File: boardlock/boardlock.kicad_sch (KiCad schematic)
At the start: 48 parts, among them U1 ESP32-S3-WROOM-1

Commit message: footprints finished for now
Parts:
- removed U1: ESP32-S3-WROOM-1, PCM_Espressif:ESP32-S3-WROOM-1, symbol PCM_Espressif:ESP32-S3-WROOM-1
- added U10: ESP32-S3-WROOM-1, espressif-kicad:ESP32-S3-WROOM-1, symbol Espressif:ESP32-S3-WROOM-1
- H1, H2, H3, H4: footprint (none) -> MountingHole:MountingHole_2.2mm_M2
- TP10, TP11, TP12, TP13, TP14, TP15, TP16, TP17, TP18, TP19, TP20, TP22, TP23, TP24, TP25, TP26, TP27, TP28, TP29, TP31, TP32, TP35, TP36, TP37, TP38, TP39, TP4, TP41, TP42, TP7, TP8, TP9: footprint (none) -> TestPoint:TestPoint_Pad_D1.0mm
- TP30, TP33, TP34, TP5: footprint TestPoint:TestPoint_Plated_Hole_D3.0mm -> TestPoint:TestPoint_Pad_D1.0mm
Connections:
- net +3V3: now also U10.2 (3V3)
- net GND: now also U10.1 (GND), U10.40 (GND), U10.41 (GND)
- net M_AUDIO_SD_MODE: now also U10.9 (GPIO16/U0CTS/ADC2_CH5/XTAL_32K_N)
- net M_BOOST_EN: now also U10.24 (GPIO47/SPICLK_P/SUBSPICLK_P_DIFF)
- net M_BOOT: now also U10.27 (GPIO0/BOOT)
- net M_BUTTON_EXT1: now also U10.39 (GPIO1/TOUCH1/ADC1_CH0)
- net M_BUTTON_EXT2: now also U10.38 (GPIO2/TOUCH2/ADC1_CH1)
- net M_BUTTON_INT: now also U10.31 (GPIO38/FSPIWP/SUBSPIWP)
- net M_BUZZER: now also U10.25 (GPIO48/SPICLK_N/SUBSPICLK_N_DIFF)
- net M_FUEL_GPOUT: now also U10.8 (GPIO15/U0RTS/ADC2_CH4/XTAL_32K_P)
- net M_GPS_EXTINT: now also U10.23 (GPIO21)
- net M_GPS_POWER: now also U10.22 (GPIO14/TOUCH14/ADC2_CH3/FSPIWP/FSPIDQS/SUBSPIWP)
- net M_HEARTBEAT: now also U10.30 (SPIDQS/GPIO37/FSPIQ/SUBSPIQ)
- net M_I2C_SCL: now also U10.17 (GPIO9/TOUCH9/ADC1_CH8/FSPIHD/SUBSPIHD)
- net M_I2C_SDA: now also U10.12 (GPIO8/TOUCH8/ADC1_CH7/SUBSPICS1)
- net M_I2S_BCLK: now also U10.6 (GPIO6/TOUCH6/ADC1_CH5)
- net M_I2S_Data_Out: now also U10.5 (GPIO5/TOUCH5/ADC1_CH4)
- net M_I2S_LRC: now also U10.7 (GPIO7/TOUCH7/ADC1_CH6)
- net M_IMU_INT2: now also U10.28 (SPIIO6/GPIO35/FSPID/SUBSPID)
- net M_IMU_POWER: now also U10.4 (GPIO4/TOUCH4/ADC1_CH3)
- net M_RGB_B: now also U10.35 (MTMS/GPIO42)
- net M_RGB_G: now also U10.34 (MTDI/GPIO41/CLK_OUT1)
- net M_RGB_R: now also U10.33 (MTDO/GPIO40/CLK_OUT2)
- net M_RST_N: now also U10.3 (EN)
- net M_SPI_CLK: now also U10.20 (GPIO12/TOUCH12/ADC2_CH1/FSPICLK/FSPIIO6/SUBSPICLK)
- net M_SPI_CS: now also U10.18 (GPIO10/TOUCH10/ADC1_CH9/FSPICS0/FSPIIO4/SUBSPICS0)
- net M_SPI_MISO: now also U10.21 (GPIO13/TOUCH13/ADC2_CH2/FSPIQ/FSPIIO7/SUBSPIQ)
- net M_SPI_MOSI: now also U10.19 (GPIO11/TOUCH11/ADC2_CH0/FSPID/FSPIIO5/SUBSPID)
- net M_UART_RX: now also U10.11 (GPIO18/U1RXD/ADC2_CH7/CLK_OUT3)
- net M_UART_TX: now also U10.10 (GPIO17/U1TXD/ADC2_CH6)
- net M_USB_D+: now also U10.14 (GPIO20/U1CTS/ADC2_CH9/CLK_OUT1/USB_D+)
- net M_USB_D-: now also U10.13 (GPIO19/U1RTS/ADC2_CH8/CLK_OUT2/USB_D-)
- net at TP31.1: now also U10.37 (U0TXD/GPIO43/CLK_OUT1)
- net at TP33.1: now also U10.16 (GPIO46)
- net at TP34.1: now also U10.15 (GPIO3/TOUCH3/ADC1_CH2)
- net at TP30.1: now also U10.26 (GPIO45)
- net at TP6.1: now also U10.29 (SPIIO7/GPIO36/FSPICLK/SUBSPICLK)
- net at TP5.1: now also U10.32 (MTCK/GPIO39/CLK_OUT3/SUBSPICS1)
- net at TP32.1: now also U10.36 (U0RXD/GPIO44/CLK_OUT2)

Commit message: Nick PCB edits
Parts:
- added R? (x2): 0, Resistor_SMD:R_0805_2012Metric_Pad1.20x1.40mm_HandSolder, symbol Device:R_US
- added TP40, TP43: TestPoint, TestPoint:TestPoint_Pad_D1.0mm, symbol Connector:TestPoint
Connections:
- net M_BATT_CHARGE_N_CHG: now also R?.2, TP40.1
- net M_BATT_CHARGE_N_PGOOD: now also R?.2, TP43.1
- net at TP33.1, U10.16 (GPIO46): now also R?.1
- net at TP30.1, U10.26 (GPIO45): now also R?.1
- no-connect marks 2 -> 0
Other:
- moved on the sheet: TP30, TP33
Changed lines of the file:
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@@
   (junction (at 213.36 95.25) (diameter 0) (color 0 0 0 0)
   )
+  (junction (at 208.28 137.16) (diameter 0) (color 0 0 0 0)
+  )
   (junction (at 213.36 106.68) (diameter 0) (color 0 0 0 0)
   )
@@
   (junction (at 124.46 45.72) (diameter 0) (color 0 0 0 0)
   )
+  (junction (at 208.28 134.62) (diameter 0) (color 0 0 0 0)
+  )
+  (junction (at 219.71 134.62) (diameter 0) (color 0 0 0 0)
+  )
   (junction (at 113.03 45.72) (diameter 0) (color 0 0 0 0)
   )
-  (no_connect (at 43.18 34.29))
-  (no_connect (at 40.64 31.75))
+  (junction (at 219.71 137.16) (diameter 0) (color 0 0 0 0)
+  )
   (wire (pts (xy 80.01 142.24) (xy 88.9 142.24))
     (stroke (width 0) (type default))
   )
+  (wire (pts (xy 219.71 134.62) (xy 218.44 134.62))
+    (stroke (width 0) (type default))
+  )
   (wire (pts (xy 180.34 71.12) (xy 182.88 71.12))
     (stroke (width 0) (type default))
   )
+  (wire (pts (xy 220.98 134.62) (xy 219.71 134.62))
+    (stroke (width 0) (type default))
+  )
   (wire (pts (xy 180.34 114.3) (xy 189.23 114.3))
     (stroke (width 0) (type default))
@@
     (stroke (width 0) (type default))
   )
+  (wire (pts (xy 208.28 134.62) (xy 210.82 134.62))
+    (stroke (width 0) (type default))
+  )
   (wire (pts (xy 113.03 45.72) (xy 113.03 48.26))
     (stroke (width 0) (type default))
   )
+  (wire (pts (xy 220.98 137.16) (xy 219.71 137.16))
+    (stroke (width 0) (type default))
+  )
   (wire (pts (xy 180.34 104.14) (xy 189.23 104.14))
     (stroke (width 0) (type default))
@@
     (stroke (width 0) (type default))
   )
+  (wire (pts (xy 219.71 137.16) (xy 219.71 138.43))
+    (stroke (width 0) (type default))
+  )
   (wire (pts (xy 36.83 78.74) (xy 35.56 78.74))
     (stroke (width 0) (type default))
@@
     (stroke (width 0) (type default))
   )
+  (wire (pts (xy 219.71 137.16) (xy 218.44 137.16))
+    (stroke (width 0) (type default))
+  )
+  (wire (pts (xy 208.28 134.62) (xy 208.28 133.35))
+    (stroke (width 0) (type default))
+  )
   (wire (pts (xy 180.34 109.22) (xy 223.52 109.22))
     (stroke (width 0) (type default))
   )
-  (wire (pts (xy 180.34 137.16) (xy 189.23 137.16))
+  (wire (pts (xy 180.34 137.16) (xy 208.28 137.16))
     (stroke (width 0) (type default))
   )
@@
     (stroke (width 0) (type default))
   )
+  (wire (pts (xy 208.28 137.16) (xy 210.82 137.16))
+    (stroke (width 0) (type default))
+  )
   (wire (pts (xy 180.34 142.24) (xy 189.23 142.24))
     (stroke (width 0) (type default))
@@
     (stroke (width 0) (type default))
   )
+  (wire (pts (xy 219.71 134.62) (xy 219.71 133.35))
+    (stroke (width 0) (type default))
+  )
   (wire (pts (xy 252.73 127) (xy 254 127))
     (stroke (width 0) (type default))
@@
     (stroke (width 0) (type default))
   )
-  (wire (pts (xy 180.34 134.62) (xy 189.23 134.62))
+  (wire (pts (xy 180.34 134.62) (xy 208.28 134.62))
+    (stroke (width 0) (type default))
+  )
+  (wire (pts (xy 208.28 137.16) (xy 208.28 138.43))
     (stroke (width 0) (type default))
   )
@@
     )
   )
-  (global_label "M_BATT_CHARGE_N_CHG" (shape input) (at 13.97 31.75 0) (fields_autoplaced)
-    (effects (font (size 1.27 1.27)) (justify left))
-    (property "Intersheetrefs" "${INTERSHEET_REFS}" (at 39.1499 31.75 0)
+  (global_label "M_BATT_CHARGE_N_CHG" (shape input) (at 220.98 134.62 0) (fields_autoplaced)
+    (effects (font (size 1.27 1.27)) (justify left))
+    (property "Intersheetrefs" "${INTERSHEET_REFS}" (at 246.1599 134.62 0)
       (effects (font (size 1.27 1.27)) (justify left) hide)
     )
@@
     )
   )
-  (global_label "M_BATT_CHARGE_N_PGOOD" (shape input) (at 13.97 34.29 0) (fields_autoplaced)
-    (effects (font (size 1.27 1.27)) (justify left))
-    (property "Intersheetrefs" "${INTERSHEET_REFS}" (at 41.7504 34.29 0)
+  (global_label "M_BATT_CHARGE_N_PGOOD" (shape input) (at 220.98 137.16 0) (fields_autoplaced)
+    (effects (font (size 1.27 1.27)) (justify left))
+    (property "Intersheetrefs" "${INTERSHEET_REFS}" (at 248.7604 137.16 0)
       (effects (font (size 1.27 1.27)) (justify left) hide)
     )
@@
     )
   )
-  (symbol (lib_id "Connector:TestPoint") (at 189.23 137.16 270) (unit 1)
-    (in_bom yes) (on_board yes) (dnp no)
-    (property "Reference" "TP33" (at 196.85 137.16 90)
-      (effects (font (size 1.27 1.27)))
-    )
-    (property "Value" "TestPoint" (at 204.47 137.16 90)
-      (effects (font (size 1.27 1.27)))
-    )
-    (property "Footprint" "TestPoint:TestPoint_Pad_D1.0mm" (at 189.23 142.24 0)
-      (effects (font (size 1.27 1.27)) hide)
-    )
-    (property "Datasheet" "~" (at 189.23 142.24 0)
+  (symbol (lib_id "Connector:TestPoint") (at 208.28 138.43 180) (unit 1)
+    (in_bom yes) (on_board yes) (dnp no)
+    (property "Reference" "TP33" (at 208.28 146.05 90)
+      (effects (font (size 1.27 1.27)))
+    )
+    (property "Value" "TestPoint" (at 208.28 153.67 90)
+      (effects (font (size 1.27 1.27)) hide)
+    )
+    (property "Footprint" "TestPoint:TestPoint_Pad_D1.0mm" (at 203.2 138.43 0)
+      (effects (font (size 1.27 1.27)) hide)
+    )
+    (property "Datasheet" "~" (at 203.2 138.43 0)
       (effects (font (size 1.27 1.27)) hide)
     )
@@
     )
   )
+  (symbol (lib_id "Connector:TestPoint") (at 219.71 138.43 180) (unit 1)
+    (in_bom yes) (on_board yes) (dnp no)
+    (property "Reference" "TP43" (at 219.71 146.05 90)
+      (effects (font (size 1.27 1.27)))
+    )
+    (property "Value" "TestPoint" (at 219.71 153.67 90)
+      (effects (font (size 1.27 1.27)) hide)
+    )
+    (property "Footprint" "TestPoint:TestPoint_Pad_D1.0mm" (at 214.63 138.43 0)
+      (effects (font (size 1.27 1.27)) hide)
+    )
+    (property "Datasheet" "~" (at 214.63 138.43 0)
+      (effects (font (size 1.27 1.27)) hide)
+    )
+    (pin "1")
+    (instances
+      (project "boardlock"
+        (path "/e1fc29ce-837e-4062-84d8-c7e423f9eab9"
+          (reference "TP43") (unit 1)
+        )
+      )
+    )
+  )
   (symbol (lib_id "Connector:TestPoint") (at 254 91.44 270) (unit 1)
     (in_bom yes) (on_board yes) (dnp no)
@@
     )
   )
-  (symbol (lib_id "Connector:TestPoint") (at 189.23 134.62 270) (unit 1)
-    (in_bom yes) (on_board yes) (dnp no)
-    (property "Reference" "TP30" (at 196.85 134.62 90)
-      (effects (font (size 1.27 1.27)))
-    )
-    (property "Value" "TestPoint" (at 204.47 134.62 90)
-      (effects (font (size 1.27 1.27)))
-    )
-    (property "Footprint" "TestPoint:TestPoint_Pad_D1.0mm" (at 189.23 139.7 0)
-      (effects (font (size 1.27 1.27)) hide)
-    )
-    (property "Datasheet" "~" (at 189.23 139.7 0)
+  (symbol (lib_id "Connector:TestPoint") (at 208.28 133.35 0) (unit 1)
+    (in_bom yes) (on_board yes) (dnp no)
+    (property "Reference" "TP30" (at 208.28 125.73 90)
+      (effects (font (size 1.27 1.27)))
+    )
+    (property "Value" "TestPoint" (at 208.28 118.11 90)
+      (effects (font (size 1.27 1.27)) hide)
+    )
+    (property "Footprint" "TestPoint:TestPoint_Pad_D1.0mm" (at 213.36 133.35 0)
+      (effects (font (size 1.27 1.27)) hide)
+    )
+    (property "Datasheet" "~" (at 213.36 133.35 0)
       (effects (font (size 1.27 1.27)) hide)
     )
@@
         (path "/e1fc29ce-837e-4062-84d8-c7e423f9eab9"
           (reference "H1") (unit 1)
+        )
+      )
+    )
+  )
+  (symbol (lib_id "Device:R_US") (at 214.63 137.16 90) (unit 1)
+    (in_bom yes) (on_board yes) (dnp no)
+    (property "Reference" "R?" (at 213.36 139.7 90)
+      (effects (font (size 1.27 1.27)))
+    )
+    (property "Value" "0" (at 217.17 139.7 90)
+      (effects (font (size 1.27 1.27)))
+    )
+    (property "Footprint" "Resistor_SMD:R_0805_2012Metric_Pad1.20x1.40mm_HandSolder" (at 214.884 136.144 90)
+      (effects (font (size 1.27 1.27)) hide)
+    )
+    (property "Datasheet" "~" (at 214.63 137.16 0)
+      (effects (font (size 1.27 1.27)) hide)
+    )
+    (pin "1")
+    (pin "2")
+    (instances
+      (project "boardlock"
+        (path "/e1fc29ce-837e-4062-84d8-c7e423f9eab9/a05f4dcd-7a18-4529-a05e-43353e81fbf8"
+          (reference "R?") (unit 1)
+        )
+        (path "/e1fc29ce-837e-4062-84d8-c7e423f9eab9"
+          (reference "R27") (unit 1)
+        )
+      )
+    )
+  )
+  (symbol (lib_id "Connector:TestPoint") (at 219.71 133.35 0) (unit 1)
+    (in_bom yes) (on_board yes) (dnp no)
+    (property "Reference" "TP40" (at 219.71 125.73 90)
+      (effects (font (size 1.27 1.27)))
+    )
+    (property "Value" "TestPoint" (at 219.71 118.11 90)
+      (effects (font (size 1.27 1.27)) hide)
+    )
+    (property "Footprint" "TestPoint:TestPoint_Pad_D1.0mm" (at 224.79 133.35 0)
+      (effects (font (size 1.27 1.27)) hide)
+    )
+    (property "Datasheet" "~" (at 224.79 133.35 0)
+      (effects (font (size 1.27 1.27)) hide)
+    )
+    (pin "1")
+    (instances
+      (project "boardlock"
+        (path "/e1fc29ce-837e-4062-84d8-c7e423f9eab9"
+          (reference "TP40") (unit 1)
         )
       )
@@
         )
       )
+    )
+  )
+  (symbol (lib_id "Device:R_US") (at 214.63 134.62 90) (unit 1)
+    (in_bom yes) (on_board yes) (dnp no)
+    (property "Reference" "R?" (at 213.36 132.08 90)
+      (effects (font (size 1.27 1.27)))
+    )
+    (property "Value" "0" (at 217.17 132.08 90)
+      (effects (font (size 1.27 1.27)))
+    )
+    (property "Footprint" "Resistor_SMD:R_0805_2012Metric_Pad1.20x1.40mm_HandSolder" (at 214.884 133.604 90)
+      (effects (font (size 1.27 1.27)) hide)
+    )
+    (property "Datasheet" "~" (at 214.63 134.62 0)
+      (effects (font (size 1.27 1.27)) hide)
+    )
+    (pin "1")
+    (pin "2")
+    (instances
+      (project "boardlock"
+        (path "/e1fc29ce-837e-4062-84d8-c7e423f9eab9/a05f4dcd-7a18-4529-a05e-43353e81fbf8"
+          (reference "R?") (unit 1)
+        )
+        (path "/e1fc29ce-837e-4062-84d8-c7e423f9eab9"
+          (reference "R26") (unit 1)
+        )
+      )

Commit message: commit
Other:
- note added: "GPIO45 and GPIO46 are strapping pins so they are being separated in case it is an issue if we use them"
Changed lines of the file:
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@@
+    (effects (font (size 1.27 1.27)) (justify left bottom))
+  )
+  (text "GPIO45 and GPIO46 are strapping pins\nso they are being separated in case\nit is an issue if we use them"
+    (at 203.2 156.21 0)
     (effects (font (size 1.27 1.27)) (justify left bottom))
   )

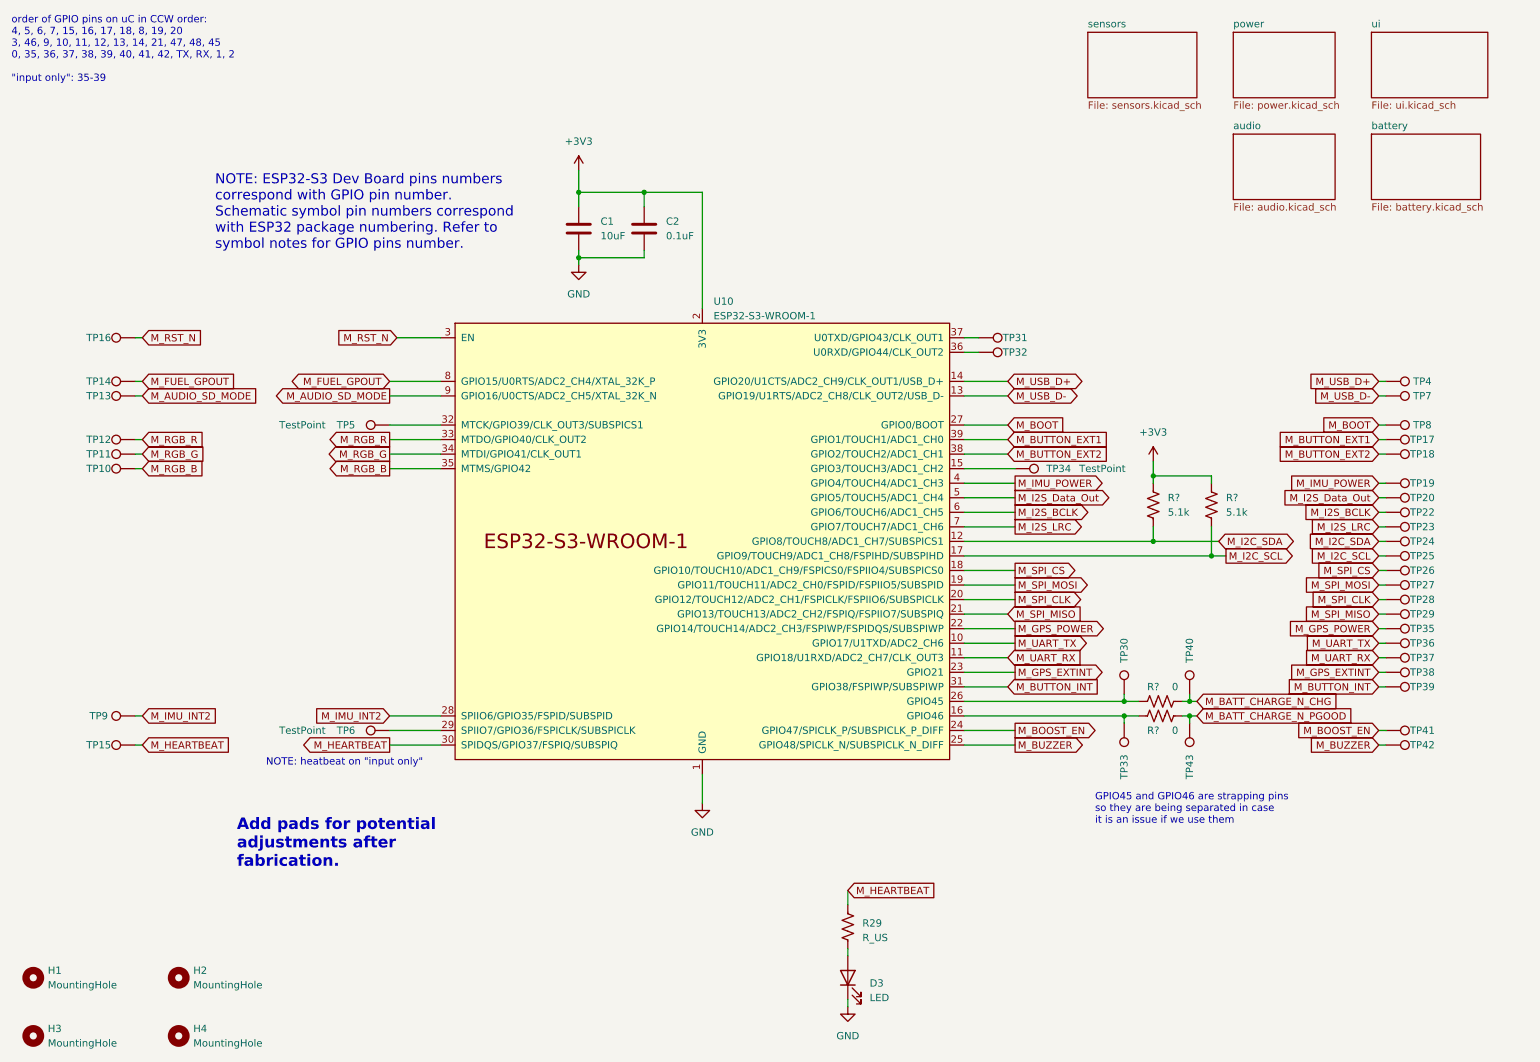
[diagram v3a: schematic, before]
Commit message: Repositioned USB C port
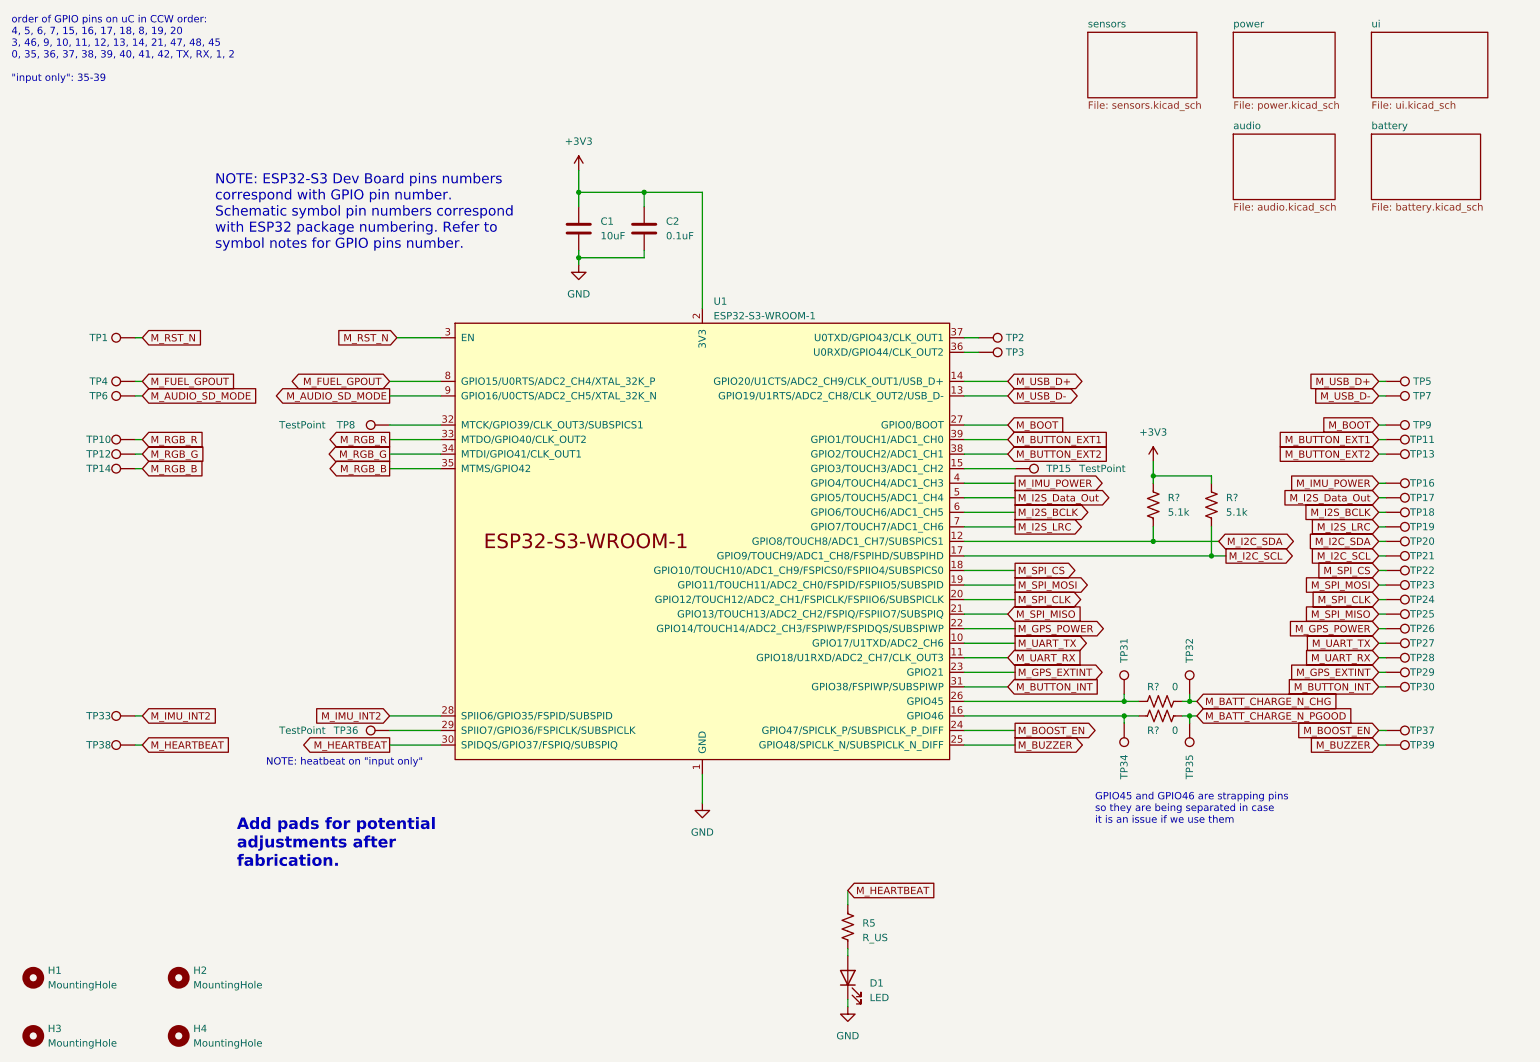
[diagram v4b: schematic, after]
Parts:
- renumbered D3 to D1, R29 to R5, TP16 to TP1, TP12 to TP10, TP17 to TP11, TP11 to TP12, TP18 to TP13, TP10 to TP14, TP34 to TP15, TP19 to TP16, TP20 to TP17, TP22 to TP18, TP23 to TP19, TP31 to TP2, TP24 to TP20, TP25 to TP21, TP26 to TP22, TP27 to TP23, TP28 to TP24, TP29 to TP25, TP35 to TP26, TP36 to TP27, TP37 to TP28, TP38 to TP29, TP32 to TP3, TP39 to TP30, TP30 to TP31, TP40 to TP32, TP9 to TP33, TP33 to TP34, TP43 to TP35, TP6 to TP36, TP41 to TP37, TP15 to TP38, TP42 to TP39, TP14 to TP4, TP4 to TP5, TP13 to TP6, TP5 to TP8, TP8 to TP9, U10 to U1
